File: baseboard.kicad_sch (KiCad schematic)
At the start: 47 parts, among them J10 AS7265X, J11 TFT_FMC, J12 SERVO1, J13 USER_GPIO, J14 TFT_SPI, J15 SERVO2, J16 FAN, J17 ADC_IN, J18 BME280, J5 POWER, J6 DCMI_CAMERA, J7 LCD_CHAR, J8 UART1, J9 UART2, Q1 BCP56, Q2 BCP56, Q3 BCP56, U2 LM2676S-5, U3 AMS1117-3.3

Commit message: snapshot prior to clearing PCB
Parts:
- removed C17: 106, Capacitor_SMD:C_0805_2012Metric_Pad1.18x1.45mm_HandSolder, symbol LM2676S-3.3_NOPB:C
- removed J11: TFT_FMC, Connector_PinHeader_2.54mm:PinHeader_2x20_P2.54mm_Vertical, symbol LM2676S-3.3_NOPB:Conn_02x20_Odd_Even
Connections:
- net PA0 renamed USER_GPIO4
- net PA10 renamed UART1_RX
- net PA15 renamed SPI1_NCS
- net PA2 renamed UART2_TX
- net PA3 renamed SERVO_OUT2
- net PA4 renamed CAM_HS
- net PA5 renamed SERVO_OUT1
- net PA6 renamed CAM_PCLK
- net PA7 renamed PWDN
- net PA8 renamed CAM_MCLK
- net PA9 renamed UART1_TX
- net PB0 renamed TFT_BL
- net PB1 renamed TFT_RS
- net PB10 renamed I2C2_SCL
- net PB11 renamed I2C2_SDA
- net PB12 renamed SPI2_NCS
- net PB13 renamed SPI2_SCK
- net PB14 renamed SPI2_MISO
- net PB15 renamed SPI2_MOSI
- net PB3 renamed SPI1_SCK
- net PB4 renamed SPI1_MISO
- net PB5 renamed SPI1_MOSI
- net PB7 renamed CAM_VS
- net PB8 renamed I2C1_SCL
- net PB9 renamed I2C1_SDA
- net PC0 renamed USER_GPIO1
- net PC13 renamed NRESET
- net PC2 renamed USER_GPIO2
- net PC3 renamed USER_GPIO3
- net PC4 renamed ADC_IN1
- net PC5 renamed ADC_IN2
- net PC6 renamed CAM_D0
- net PC7 renamed CAM_D1
- net PC8 renamed FAN_OUT
- net PD3 renamed CAM_D5
- net PD6 renamed UART2_RX
- net PE0 renamed CAM_D2
- net PE1 renamed CAM_D3
- net PE3 renamed TFT_INT
- net PE4 renamed CAM_D4
- net PE5 renamed CAM_D6
- net PE6 renamed CAM_D7
- no-connect marks 14 -> 2
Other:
- moved on the sheet: J14, R11

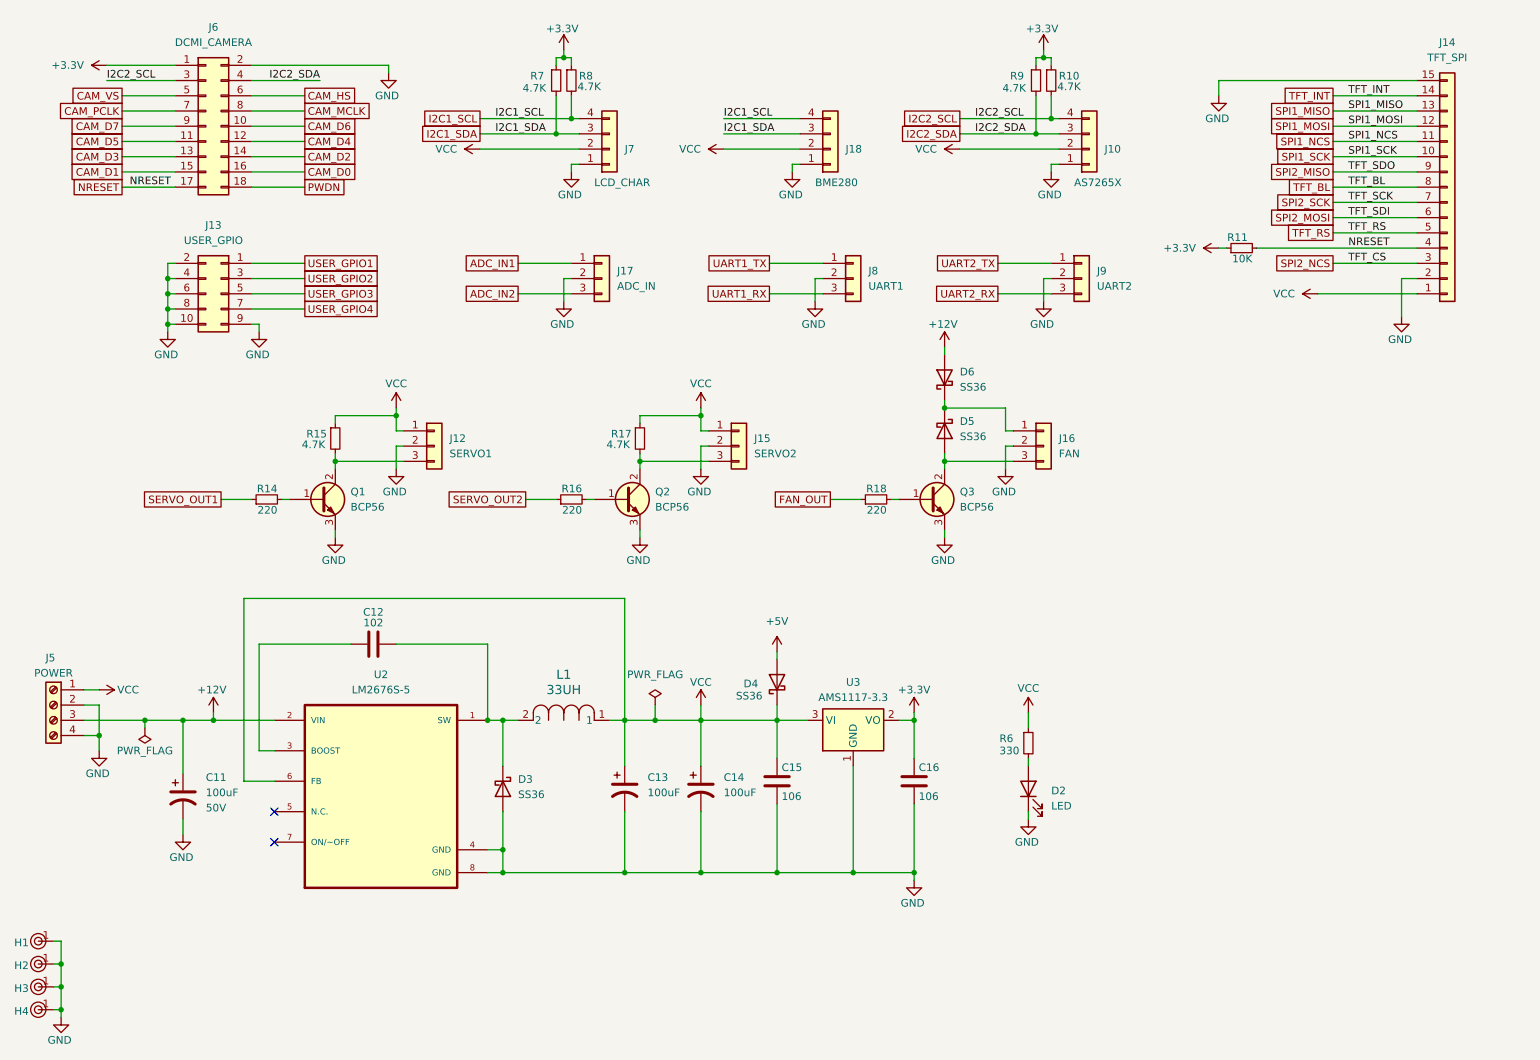
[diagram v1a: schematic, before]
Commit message: completed part placement
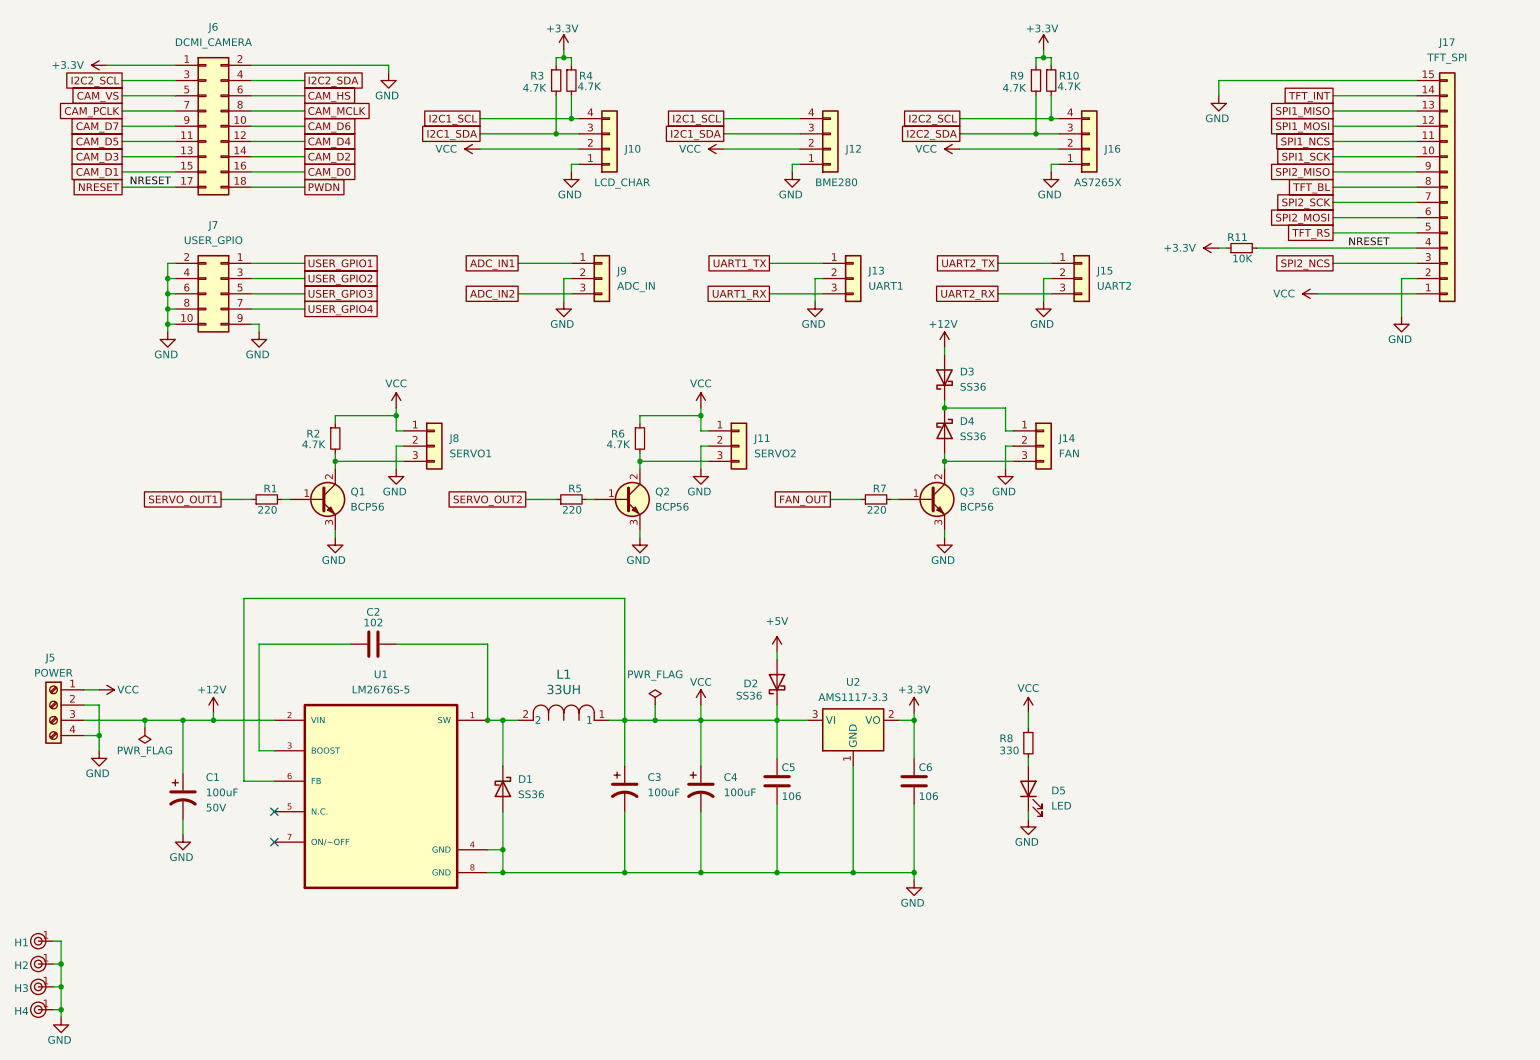
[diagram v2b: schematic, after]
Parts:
- renumbered C11 to C1, C12 to C2, C13 to C3, C14 to C4, C15 to C5, C16 to C6, D3 to D1, D4 to D2, D6 to D3, D5 to D4, D2 to D5, J7 to J10, J15 to J11, J18 to J12, J8 to J13, J16 to J14, J9 to J15, J10 to J16, J14 to J17, J13 to J7, J12 to J8, J17 to J9, R14 to R1, R15 to R2, R7 to R3, R8 to R4, R16 to R5, R17 to R6, R18 to R7, R6 to R8, U2 to U1, U3 to U2

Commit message: pass DRC without error
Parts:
- added C10: 106, Capacitor_SMD:C_0805_2012Metric_Pad1.18x1.45mm_HandSolder, symbol LM2676S-3.3_NOPB:C
- added C11, C7, C8, C9: 104, Capacitor_SMD:C_0805_2012Metric_Pad1.18x1.45mm_HandSolder, symbol LM2676S-3.3_NOPB:C
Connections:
- net +3.3V: now also C11.2
- net GND: now also C10.2, C11.1, C7.2, C8.2, C9.2
- net VCC: now also C10.1, C8.1, C9.1
- net at D3.1 (K), D4.1 (K), J14.1 (Pin_1): now also C7.1
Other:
- moved on the sheet: D5, R8
